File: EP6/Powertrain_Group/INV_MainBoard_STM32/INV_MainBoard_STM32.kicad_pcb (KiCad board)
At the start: 4 copper layers, 100 x 88 mm, 290 parts, among them J1 FX26-30P-1SV, J10 current_DC, J11 current_U, J12 current_V, J13 current_W, J2 motorSense, J3 LVBattery, J4 STDC14, J5 current_DC, J6 current_U, J7 current_V, J8 current_V, J9 CAN, SW1 TS-1187A-B-A-B, U1 OPA340NA, U10 OPA340NA, U11 OPA340NA, U12 OPA340NA, U13 LMV7219M5, U14 LMV7219M5, U15 LMV7219M5, U16 LMV7219M5, U17 LMV7219M5, U18 LMV7219M5, U19 LMV7219M5, U2 TPS5430DDAR, U20 LMV7219M5, U21 OPA340NA, U22 TCAN1042VDRQ1, U3 AMS1117-3.3, U4 STM32G474RETx, U5 CAT24C256, U6 TCAN1042VDRQ1, U7 OPA340NA, U8 OPA340NA, U9 OPA340NA, Y1 X322525MOB4SI 25Mhz, Y2 X322516MLB4SI 16MHz

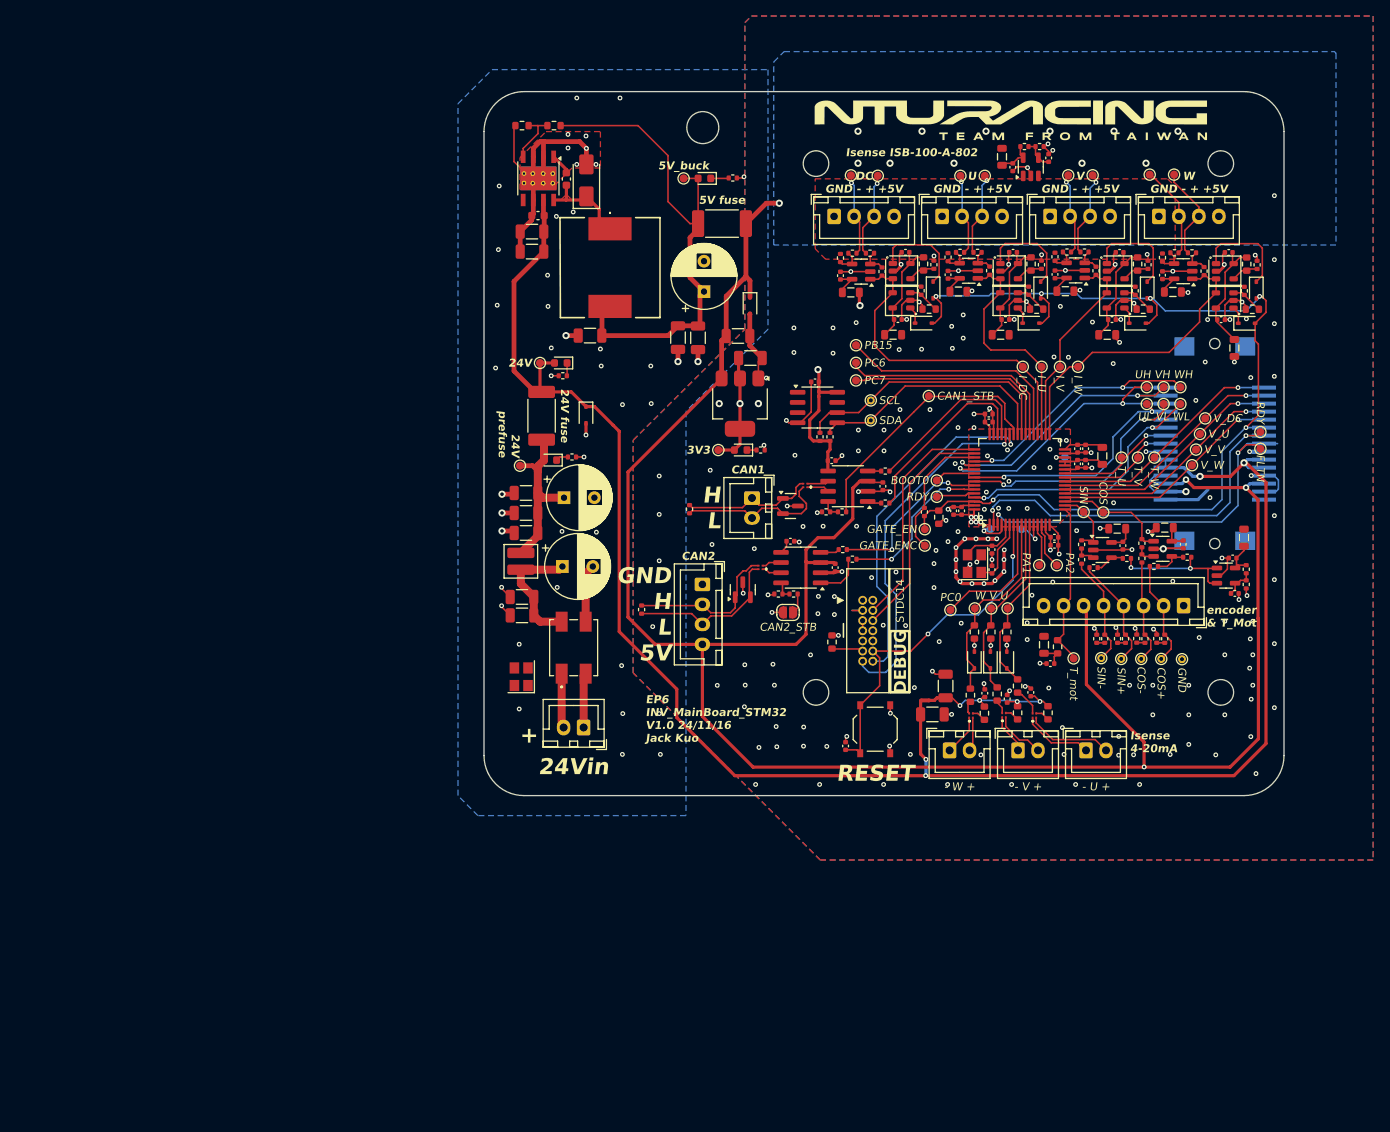
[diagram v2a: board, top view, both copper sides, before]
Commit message: update INV_MainBoard_STM32 to V2.0
big update to match new INV_GateDriver
and use H743ZI as MCU
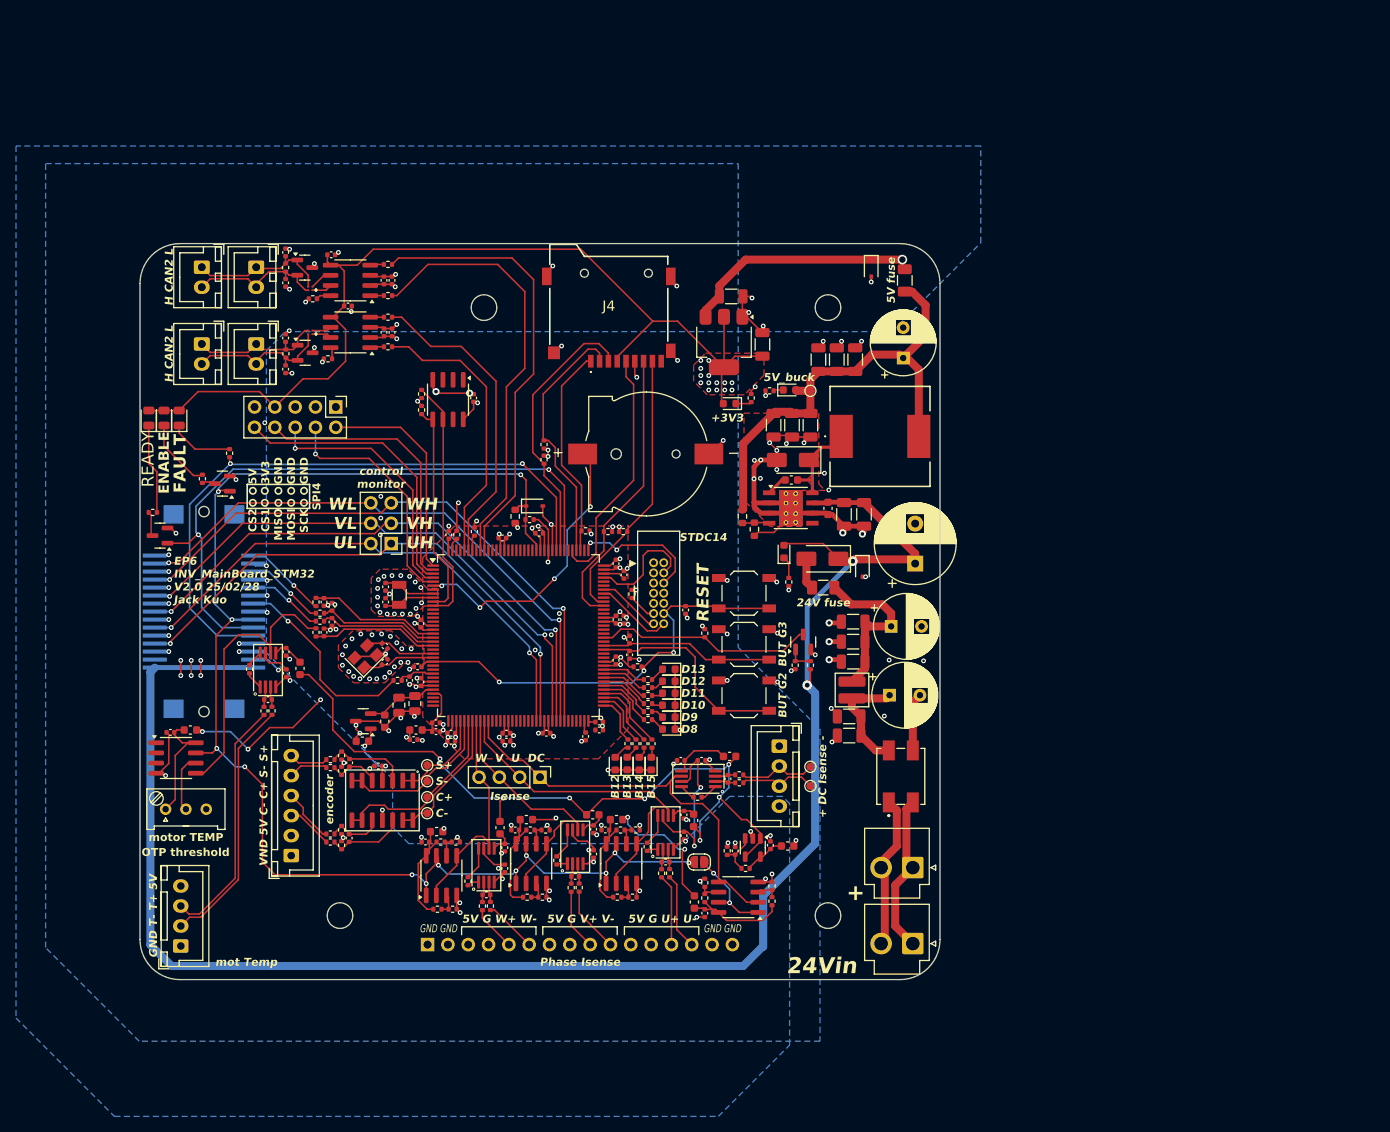
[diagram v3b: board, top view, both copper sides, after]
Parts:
- removed FB17: GZ1608D601TF, Inductor_SMD:L_0805_2012Metric
- removed FB3: GZ2012D601TF, Inductor_SMD:L_0805_2012Metric
- removed FL4, FL5, FL6: EXC-X4CE900U, SamacSys_Parts_EP6:EXCX4CE900U
- removed H5: M4, MountingHole:MountingHole_4mm
- removed TIE1, TIE2: NetTie, NetTie:NetTie-2_SMD_Pad0.5mm
- removed TP1: 24V_prefuse, TestPoint:TestPoint_Pad_D1.0mm
- removed TP10: A1, TestPoint:TestPoint_Pad_D1.0mm
- removed TP11: A2, TestPoint:TestPoint_Pad_D1.0mm
- removed TP12: eCOS, TestPoint:TestPoint_Pad_D1.0mm
- removed TP13: B7, TestPoint:TestPoint_Pad_D1.0mm
- removed TP14: B10, TestPoint:TestPoint_Pad_D1.0mm
- removed TP15: B15, TestPoint:TestPoint_Pad_D1.0mm
- removed TP16: D2, TestPoint:TestPoint_Pad_D1.0mm
- removed TP17: C6, TestPoint:TestPoint_Pad_D1.0mm
- removed TP18: C7, TestPoint:TestPoint_Pad_D1.0mm
- removed TP19: C15, TestPoint:TestPoint_Pad_D1.0mm
- removed TP2: 24V, TestPoint:TestPoint_Pad_D1.0mm
- removed TP20: C0, TestPoint:TestPoint_Pad_D1.0mm
- removed TP21: eSIN, TestPoint:TestPoint_Pad_D1.0mm
- removed TP22: WH, TestPoint:TestPoint_Pad_D1.0mm
- removed TP23: VH, TestPoint:TestPoint_Pad_D1.0mm
- removed TP24: UH, TestPoint:TestPoint_Pad_D1.0mm
- removed TP25: Ready, TestPoint:TestPoint_Pad_D1.0mm
- removed TP26: NFLT, TestPoint:TestPoint_Pad_D1.0mm
- removed TP27: GEnC, TestPoint:TestPoint_Pad_D1.0mm
- removed TP28: CAN1_STB, TestPoint:TestPoint_Pad_D1.0mm
- removed TP29: TW, TestPoint:TestPoint_Pad_D1.0mm
- removed TP30: TV, TestPoint:TestPoint_Pad_D1.0mm
- removed TP31: TU, TestPoint:TestPoint_Pad_D1.0mm
- removed TP32: UL, TestPoint:TestPoint_Pad_D1.0mm
- removed TP33: VL, TestPoint:TestPoint_Pad_D1.0mm
- removed TP34: WL, TestPoint:TestPoint_Pad_D1.0mm
- removed TP35: GEnFb, TestPoint:TestPoint_Pad_D1.0mm
- removed TP36: IW, TestPoint:TestPoint_Pad_D1.0mm
- removed TP37: IV, TestPoint:TestPoint_Pad_D1.0mm
- removed TP38: IU, TestPoint:TestPoint_Pad_D1.0mm
- removed TP39: IDC, TestPoint:TestPoint_Pad_D1.0mm
- removed TP4: 3V3, TestPoint:TestPoint_Pad_D1.0mm
- removed TP40: IcW, TestPoint:TestPoint_Pad_D1.0mm
- removed TP41: IcV, TestPoint:TestPoint_Pad_D1.0mm
- removed TP42: IcU, TestPoint:TestPoint_Pad_D1.0mm
- removed TP43: VU, TestPoint:TestPoint_Pad_D1.0mm
- removed TP44: VDC, TestPoint:TestPoint_Pad_D1.0mm
- removed TP45: VV, TestPoint:TestPoint_Pad_D1.0mm
- removed TP46: VW, TestPoint:TestPoint_Pad_D1.0mm
- removed TP47: TM, TestPoint:TestPoint_Pad_D1.0mm
- removed TP48: GND, TestPoint:TestPoint_THTPad_D1.0mm_Drill0.5mm
- removed TP49: SCL, TestPoint:TestPoint_THTPad_D1.0mm_Drill0.5mm
- removed TP50: SDA, TestPoint:TestPoint_THTPad_D1.0mm_Drill0.5mm
- removed TP53: I_U+, TestPoint:TestPoint_Pad_D1.0mm
- removed TP54: I_U-, TestPoint:TestPoint_Pad_D1.0mm
- removed TP55: I_V+, TestPoint:TestPoint_Pad_D1.0mm
- removed TP56: I_V-, TestPoint:TestPoint_Pad_D1.0mm
- removed TP57: I_W+, TestPoint:TestPoint_Pad_D1.0mm
- removed TP58: I_W-, TestPoint:TestPoint_Pad_D1.0mm
- removed TP9: A0, TestPoint:TestPoint_Pad_D1.0mm
- removed U19, U20: LMV7219M5, PCM_Package_TO_SOT_SMD_AKL:SOT-23-5
- removed U21: OPA340NA, Package_TO_SOT_SMD:SOT-23-5
- removed U22: TCAN1042VDRQ1, Package_SO:SOIC-8_3.9x4.9mm_P1.27mm
- added BT1: 1056, nturt_kicad_lib_EP6:BAT_1056, F.Cu at (172.0, 83.3)
- added C100: 680p, Capacitor_SMD:C_0402_1005Metric, F.Cu at (174.2, 134.3)
- added C101: 680p, Capacitor_SMD:C_0402_1005Metric, F.Cu at (162.9, 136.1)
- added C102: 680p, Capacitor_SMD:C_0402_1005Metric, F.Cu at (151.8, 138.4)
- added C103: 100n, Capacitor_SMD:C_0402_1005Metric, F.Cu at (187.3, 132.2)
- added C104: 100n, Capacitor_SMD:C_0402_1005Metric, F.Cu at (182.9, 132.9)
- added C105: 100n, Capacitor_SMD:C_0402_1005Metric, F.Cu at (126.8, 108.0)
- added C106: 100n, Capacitor_SMD:C_0402_1005Metric, F.Cu at (176.1, 121.6)
- added C107: 100n, Capacitor_SMD:C_0402_1005Metric, F.Cu at (176.5, 128.4)
- added C108: 100n, Capacitor_SMD:C_0402_1005Metric, F.Cu at (165.2, 130.2)
- added C109: 100n, Capacitor_SMD:C_0402_1005Metric, F.Cu at (154.1, 132.5)
- added C112: 22p, Capacitor_SMD:C_0402_1005Metric, F.Cu at (126.7, 58.1)
- added C113: 22p, Capacitor_SMD:C_0402_1005Metric, F.Cu at (126.7, 61.9)
- added C114: 22p, Capacitor_SMD:C_0402_1005Metric, F.Cu at (126.7, 68.8)
- added C115: 22p, Capacitor_SMD:C_0402_1005Metric, F.Cu at (126.7, 72.7)
- added C116: 4u7 10v, Capacitor_SMD:C_0402_1005Metric, F.Cu at (140.0, 61.6)
- added C117: 4u7 10v, Capacitor_SMD:C_0402_1005Metric, F.Cu at (140.0, 68.1)
- added C118: 22u 25V, Capacitor_SMD:C_1206_3216Metric, F.Cu at (193.3, 71.5)
- added C119: 22u 25V, Capacitor_SMD:C_1206_3216Metric, F.Cu at (195.6, 71.5)
- added C120: 22u 25V, Capacitor_SMD:C_1206_3216Metric, F.Cu at (197.9, 71.5)
- added C60: 100n, Capacitor_SMD:C_0402_1005Metric, F.Cu at (168.0, 97.0)
- added C61: 100n, Capacitor_SMD:C_0402_1005Metric, F.Cu at (168.0, 104.0)
- added C62: 100n, Capacitor_SMD:C_0402_1005Metric, F.Cu at (147.1, 93.4)
- added C63: 100n, Capacitor_SMD:C_0402_1005Metric, F.Cu at (165.9, 116.8)
- added C64: 0u1, Capacitor_SMD:C_0402_1005Metric, F.Cu at (145.5, 116.9)
- added C65: 10u 6V, Capacitor_SMD:C_0402_1005Metric, F.Cu at (145.5, 118.0)
- added C66: 10u 6V, Capacitor_SMD:C_0402_1005Metric, F.Cu at (142.7, 119.0)
- added C67: 4u7, Capacitor_SMD:C_0402_1005Metric, F.Cu at (154.3, 119.2)
- added C85: 43p, Capacitor_SMD:C_0402_1005Metric, F.Cu at (134.6, 131.3)
- added C86: 100n, Capacitor_SMD:C_0402_1005Metric, F.Cu at (138.3, 122.3)
- added C87: 22u, Capacitor_SMD:C_0805_2012Metric, F.Cu at (140.9, 114.7)
- added C88: 22u, Capacitor_SMD:C_0805_2012Metric, F.Cu at (142.9, 114.5)
- added C91: 470n, Capacitor_SMD:C_0603_1608Metric, F.Cu at (139.1, 116.7)
- added C92: 470n, Capacitor_SMD:C_0603_1608Metric, F.Cu at (136.3, 119.2)
- added C96: 1u, Capacitor_SMD:C_0402_1005Metric, F.Cu at (124.5, 114.0)
- added C97: 3n3, Capacitor_SMD:C_0402_1005Metric, F.Cu at (142.2, 111.6)
- added C99: 680p, Capacitor_SMD:C_0402_1005Metric, F.Cu at (182.0, 123.9)
- added D21: Y LED, LED_SMD:LED_0603_1608Metric, F.Cu at (169.4, 122.0)
- added D22: G LED, LED_SMD:LED_0603_1608Metric, F.Cu at (170.9, 122.0)
- added D23: B LED, LED_SMD:LED_0603_1608Metric, F.Cu at (172.4, 122.0)
- added J14: LVBattery, Connector_JST:JST_VH_B2P-VH_1x02_P3.96mm_Vertical, F.Cu at (205.1, 144.5)
- added J15: STDC14, nturt_kicad_lib_EP6:box_header_14P_pitch127, F.Cu at (172.7, 96.9)
- added J16: SPI, Connector_PinHeader_2.54mm:PinHeader_2x05_P2.54mm_Vertical, F.Cu at (133.0, 77.4)
- added Q1: 2N7002, Package_TO_SOT_SMD:SOT-23, F.Cu at (118.8, 87.0)
- added Q2: 2N7002, Package_TO_SOT_SMD:SOT-23, F.Cu at (111.0, 93.5)
- added Q3: AO3400A, Package_TO_SOT_SMD:SOT-23, F.Cu at (191.4, 106.8)
- added R84: 15k, Resistor_SMD:R_0402_1005Metric, F.Cu at (192.3, 109.7)
- added R85: 1k, Resistor_SMD:R_0402_1005Metric, F.Cu at (190.4, 109.7)
- added R86: 2k2, Resistor_SMD:R_0402_1005Metric, F.Cu at (170.5, 119.5)
- added R87: 2k2, Resistor_SMD:R_0402_1005Metric, F.Cu at (171.5, 119.5)
- added R88: 2k2, Resistor_SMD:R_0402_1005Metric, F.Cu at (172.5, 119.5)
- added RV1: 10K, nturt_kicad_lib_EP6:Throughhole Potentiometer 3296W, F.Cu at (111.7, 127.7)
- added SW2: TS-1187A-B-A-B, Button_Switch_SMD:SW_SPST_TL3342, F.Cu at (184.0, 107.1)
- added SW3: TS-1187A-B-A-B, Button_Switch_SMD:SW_SPST_TL3342, F.Cu at (184.0, 113.5)
- added U23: REF3133AQDBZRQ1, Package_TO_SOT_SMD:SOT-23, F.Cu at (136.4, 116.7)
- C1, C2: value 0u1 -> 47u 10V; footprint Capacitor_SMD:C_0402_1005Metric -> Capacitor_SMD:C_1206_3216Metric
- C20, C21: value 47u 10V -> 100n; footprint Capacitor_SMD:C_1206_3216Metric -> Capacitor_SMD:C_0402_1005Metric
- C22, C23, C24, C25: value 10u 6V -> 100n
- C26, C27, C29, C38, C40, C41, C42, C43, C46, C47, C48, C49, C51, C52, C57, C58: value 0u1 -> 100n
- C28: value 0u1 -> 4u7
- C30: value 0u1 -> 15p
- C31: value 10u 6V -> 15p
- C33, C34: value 15p -> 27p
- C44, C45: value 0u1 -> 2u2
- C54: value 0u1 -> 100uF 27V; footprint Capacitor_SMD:C_0402_1005Metric -> Capacitor_THT:CP_Radial_D10.0mm_P5.00mm
- C55, C56: value 10u 35V -> 4u7; footprint Capacitor_SMD:C_1206_3216Metric -> Capacitor_SMD:C_0402_1005Metric
- C59: value 0u1 -> 43p
- D1: value RED 24VpreFuse -> GREEN LED; footprint LED_SMD:LED_0603_1608Metric -> LED_SMD:LED_0805_2012Metric
- D10: value 1N4148W -> G LED; footprint Diode_SMD:D_SOD-323 -> LED_SMD:LED_0603_1608Metric
- D11: value 1N4148W -> R LED; footprint Diode_SMD:D_SOD-323 -> LED_SMD:LED_0603_1608Metric
- D12: value 1N4148W -> RED 3V3; footprint Diode_SMD:D_SOD-323 -> LED_SMD:LED_0603_1608Metric
- D13: value 1N4148W -> B LED; footprint Diode_SMD:D_SOD-323 -> LED_SMD:LED_0603_1608Metric
- D14: value 1N4148W -> Y LED; footprint Diode_SMD:D_SOD-323 -> LED_SMD:LED_0603_1608Metric
- D15: value 1N4148W -> B5818WS
- D16: value 1N4148W -> W LED; footprint Diode_SMD:D_SOD-323 -> LED_SMD:LED_0603_1608Metric
- D18, D20: value 3.7V BZT52C3V9S -> R LED; footprint Diode_SMD:D_SOD-323 -> LED_SMD:LED_0603_1608Metric
- D19: value 3.7V BZT52C3V9S -> SS54; footprint Diode_SMD:D_SOD-323 -> Diode_SMD:D_SMA
- D7: value RED 3V3 -> WHITE LED; footprint LED_SMD:LED_0603_1608Metric -> LED_SMD:LED_0805_2012Metric
- D9: value 1N4148W -> RED; footprint Diode_SMD:D_SOD-323 -> LED_SMD:LED_0805_2012Metric
- F1: footprint Fuse:Fuse_2512_6332Metric_Pad1.52x3.35mm_HandSolder -> Fuse:Fuse_1206_3216Metric
- F2: value 0.5A -> 1A; footprint Fuse:Fuse_2512_6332Metric_Pad1.52x3.35mm_HandSolder -> Fuse:Fuse_1206_3216Metric
- FB1, FB10, FB11, FB13, FB15, FB2, FB4, FB5, FB6, FB7, FB8, FB9: value GZ2012D601TF -> GZ1608D601TF; footprint Inductor_SMD:L_0805_2012Metric -> Capacitor_SMD:C_0603_1608Metric
- J10: value current_DC -> CAN; footprint Connector_JST:JST_XH_B4B-XH-A_1x04_P2.50mm_Vertical -> Connector_JST:JST_XH_B2B-XH-A_1x02_P2.50mm_Vertical
- J11: value current_U -> CAN
- J12: value current_V -> CAN
- J13: value current_W -> motorTemp; footprint Connector_JST:JST_XH_B2B-XH-A_1x02_P2.50mm_Vertical -> Connector_JST:JST_XH_B4B-XH-A_1x04_P2.50mm_Vertical
- J2: footprint Connector_JST:JST_XH_B8B-XH-A_1x08_P2.50mm_Vertical -> Connector_JST:JST_XH_B6B-XH-A_1x06_P2.50mm_Vertical
- J3: footprint Connector_JST:JST_XH_B2B-XH-A_1x02_P2.50mm_Vertical -> Connector_JST:JST_VH_B2P-VH_1x02_P3.96mm_Vertical
- J4: value STDC14 -> MSD-4-A; footprint nturt_kicad_lib_EP6:box_header_14P_pitch127 -> SamacSys_Parts_EP6:MSD4A
- J6: value current_U -> to PhaseIsense; footprint Connector_JST:JST_XH_B4B-XH-A_1x04_P2.50mm_Vertical -> Connector_PinHeader_2.54mm:PinHeader_1x16_P2.54mm_Horizontal; moved to B.Cu
- J7: value current_V -> phase control monitor; footprint Connector_JST:JST_XH_B4B-XH-A_1x04_P2.50mm_Vertical -> Connector_PinHeader_2.54mm:PinHeader_2x03_P2.54mm_Vertical
- J8: value current_V -> current; footprint Connector_JST:JST_XH_B4B-XH-A_1x04_P2.50mm_Vertical -> Connector_PinHeader_2.54mm:PinHeader_1x04_P2.54mm_Vertical
- JP1: value CAN2STB -> DC OCP
- L3: footprint SamacSys_Parts:SRR1260A220M -> SamacSys_Parts_EP6:SRR1260A220M
- R1: value 10k -> 510R
- R11: value 1k -> 10k
- R12: value 100R -> 4k7; footprint Resistor_SMD:R_0603_1608Metric -> Resistor_SMD:R_0402_1005Metric
- R13, R14, R18, R28, R6, R68: value 10k -> 2k2
- R15, R16, R70, R71: value 100R -> 20R
- R17: value 100R -> 90R
- R19, R20, R21, R22: value 10k -> 10k 0.1%
- R2: value 10k -> 100R
- R23: value 20k -> 20k 0.1%
- R24: value 20k -> 4k7
- R25, R26: value 20k -> 10k 0.1%
- R27: value 15k -> 2k2
- R29, R55: value 10k -> 2k4
- R3: value 20k -> 1k
- R30, R31, R50: value 15k -> 10k
- R33, R51, R58: value 10k -> 28k
- R34, R38: value 15k -> 20k 0.1%
- R35, R39, R43, R47: value 15k -> 100R
- R36, R40, R44, R48: value 20k -> 100R
- R37: value 20k -> 10M
- R41, R45, R49: value 20k -> 100k
- R42, R46: value 15k -> 4k7
- R5: value 1k -> 10k; footprint Resistor_SMD:R_0603_1608Metric -> Resistor_SMD:R_0402_1005Metric
- R52, R57, R61, R64: value 45k3 -> 10k; footprint Resistor_SMD:R_0603_1608Metric -> Resistor_SMD:R_0402_1005Metric
- R53, R56, R60: value 45k3 -> 28k; footprint Resistor_SMD:R_0603_1608Metric -> Resistor_SMD:R_0402_1005Metric
- R62: value 10k -> 4k7
- R65: value 45k3 -> 10M; footprint Resistor_SMD:R_0603_1608Metric -> Resistor_SMD:R_0402_1005Metric
- R67: value 120R -> 10k
- R72: value 120R -> 90R
- R73: value 100R -> 10k
- R75: value 150R -> 100R; footprint Resistor_SMD:R_0603_1608Metric -> Resistor_SMD:R_0402_1005Metric
- R76: value 150R -> 1k; footprint Resistor_SMD:R_0603_1608Metric -> Resistor_SMD:R_0402_1005Metric
- R77: value 150R -> 2k2; footprint Resistor_SMD:R_0603_1608Metric -> Resistor_SMD:R_0402_1005Metric
- R78, R80: value 100R -> 2k2; footprint Resistor_SMD:R_0603_1608Metric -> Resistor_SMD:R_0402_1005Metric
- R79: value 100R -> 10k; footprint Resistor_SMD:R_0603_1608Metric -> Resistor_SMD:R_0402_1005Metric
- R81, R82: value 100R -> 1k; footprint Resistor_SMD:R_0603_1608Metric -> Resistor_SMD:R_0402_1005Metric
- R83: value 100R -> 20k 0.1%; footprint Resistor_SMD:R_0603_1608Metric -> Resistor_SMD:R_0402_1005Metric
- SW1: footprint Button_Switch_SMD:SW_Push_1P1T_XKB_TS-1187A -> Button_Switch_SMD:SW_SPST_TL3342
- TP5, TP6, TP7, TP8: footprint TestPoint:TestPoint_THTPad_D1.0mm_Drill0.5mm -> TestPoint:TestPoint_Pad_D1.0mm
- TP51: value I_DC+ -> I_W+
- TP52: value I_DC- -> I_W-
- U1: value OPA340NA -> STM32H743ZITx; footprint Package_TO_SOT_SMD:SOT-23-5 -> Package_QFP:LQFP-144_20x20mm_P0.5mm
- U10, U11, U12: value OPA340NA -> LM2903; footprint Package_TO_SOT_SMD:SOT-23-5 -> Package_SO:SOIC-8_3.9x4.9mm_P1.27mm
- U13, U15: value LMV7219M5 -> LM2903; footprint PCM_Package_TO_SOT_SMD_AKL:SOT-23-5 -> Package_SO:SOIC-8_3.9x4.9mm_P1.27mm
- U14: value LMV7219M5 -> INA333AIDGK; footprint PCM_Package_TO_SOT_SMD_AKL:SOT-23-5 -> PCM_Package_SO_AKL:MSOP-8_3x3mm_P0.65mm
- U16: value LMV7219M5 -> LM324D; footprint PCM_Package_TO_SOT_SMD_AKL:SOT-23-5 -> PCM_Package_SO_AKL:SOIC-14_3.9x8.7mm_P1.27mm
- U17: value LMV7219M5 -> AMS1117-3.3; footprint PCM_Package_TO_SOT_SMD_AKL:SOT-23-5 -> Package_TO_SOT_SMD:SOT-223-3_TabPin2
- U18: value LMV7219M5 -> OPA340NA; footprint PCM_Package_TO_SOT_SMD_AKL:SOT-23-5 -> Package_TO_SOT_SMD:SOT-23-5
- U3: value AMS1117-3.3 -> INA333AIDGK; footprint Package_TO_SOT_SMD:SOT-223-3_TabPin2 -> PCM_Package_SO_AKL:MSOP-8_3x3mm_P0.65mm
- U4: value STM32G474RETx -> TCAN1042VDRQ1; footprint Package_QFP:LQFP-64_10x10mm_P0.5mm -> Package_SO:SOIC-8_3.9x4.9mm_P1.27mm
- U7, U8, U9: value OPA340NA -> INA333AIDGK; footprint Package_TO_SOT_SMD:SOT-23-5 -> PCM_Package_SO_AKL:MSOP-8_3x3mm_P0.65mm
- Y1: value X322525MOB4SI 25Mhz -> 48MHz YF4048M00033T8188103
- Y2: value X322516MLB4SI 16MHz -> 32.768kHz Q13FC13500004; footprint Crystal:Crystal_SMD_3225-4Pin_3.2x2.5mm -> Crystal:Crystal_SMD_3215-2Pin_3.2x1.5mm
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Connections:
- C1 pad 1: Net-(U1-V+) -> +5V
- C2 pad 1: Net-(U1--) -> +3V3
- C20 pad 1: +5V -> /Isense&motT_OCP&OTP/filt3V3
- C21 pad 1: +3V3 -> +5V
- C30 pad 1: /MCU/3V3_REF -> /MCU/OSC32_OUT
- C31 pad 1: /MCU/3V3_REF -> /MCU/OSC32_IN
- C32 pad 1: /MCU/SWD_NRST -> /MCU/NRST
- C33 pad 1: /MCU/OSC_IN -> /MCU/OSC_OUT
- C33 pad 2: /MCU/CrystalGND -> GND
- C34 pad 1: /MCU/OSC_OUT -> /MCU/OSC_IN
- C34 pad 2: /MCU/CrystalGND -> GND
- C38 pad 1: Net-(U7-V+) -> /T_filt_mot
- C39 pad 1: Net-(U8-V+) -> /MCU/BUT_G3
- C40 pad 1: Net-(U9-V+) -> +5V
- C41 pad 1: Net-(U10-V+) -> +5V
- C42 pad 1: Net-(U11-V+) -> +5V
- C43 pad 1: Net-(U12-V+) -> +5V
- C44 pad 1: Net-(U13-V+) -> /MCU/VCAP1
- C45 pad 1: Net-(U13-V+) -> /MCU/VCAP2
- C46 pad 1: Net-(U15-V+) -> /Isense&motT_OCP&OTP/OCPnode/filt3V3
- C47 pad 1: Net-(U15-V+) -> /Isense&motT_OCP&OTP/OCPnode1/filt3V3
- C48 pad 1: Net-(U17-V+) -> /Isense&motT_OCP&OTP/OCPnode2/filt3V3
- C49 pad 1: Net-(U17-V+) -> /Isense&motT_OCP&OTP/OCPnode3/filt3V3
- C50 pad 1: Net-(U19-V+) -> /MCU/NRST
- C51 pad 1: Net-(U19-V+) -> +3V3
- C52 pad 1: Net-(C52-Pad1) -> /T_filt_W
- C53 pad 1: Net-(U21-V+) -> /MCU/BUT_G2
- C54 pad 1: Net-(U21--) -> +24V
- C55 pad 1: +24V -> +3V3
- C56 pad 1: /Isense_OCP/+24V_4-20mA -> +3V3
- C57 pad 1: /Isense_OCP/+24V_4-20mA -> /T_filt_V
- C58 pad 1: /Isense_OCP/+24V_4-20mA -> /T_filt_U
- C59 pad 1: /Isense_OCP/+24V_4-20mA -> Net-(U16A-+)
- C59 pad 2: GND -> Net-(U16B-+)
- D1 pad 2: /Power/+24V_prefuse -> +3V3
- D10 pad 1: Net-(D10-K) -> GND
- D10 pad 2: /GATE_EN -> Net-(D10-A)
- D11 pad 1: Net-(D11-K) -> GND
- D11 pad 2: /GATE_EN -> Net-(D11-A)
- D12 pad 2: /GATE_EN -> +3V3
- D13 pad 1: Net-(D13-K) -> GND
- D13 pad 2: /GATE_EN -> Net-(D13-A)
- D14 pad 1: Net-(D14-K) -> GND
- D14 pad 2: /GATE_EN -> Net-(D14-A)
- D15 pad 1: Net-(D15-K) -> /GATE_EN
- D15 pad 2: /GATE_EN -> /OCPFLTN
- D16 pad 1: Net-(D16-K) -> GND
- D16 pad 2: /GATE_EN -> Net-(D16-A)
- D17 pad 1: /MCU/CAN2L -> /Peripherals/CAN1L
- D17 pad 2: /MCU/CAN2H -> /Peripherals/CAN1H
- D18 pad 1: /Isense_OCP/Isense_current_U -> GND
- D18 pad 2: GND -> Net-(D18-A)
- D19 pad 1: /Isense_OCP/Isense_current_V -> +24V
- D19 pad 2: GND -> Net-(D19-A)
- D20 pad 1: /Isense_OCP/Isense_current_W -> GND
- D20 pad 2: GND -> Net-(D20-A)
- D8 pad 1: /MCU/CAN1L -> /Peripherals/CAN2L
- D8 pad 2: /MCU/CAN1H -> /Peripherals/CAN2H
- D9 pad 2: /GATE_EN -> +3V3
- F1 pad 2: +24V -> Net-(D19-A)
- FB1 pad 2: Net-(U1-V+) -> /Isense&motT_OCP&OTP/OCPnode/filt3V3
- FB10 pad 1: +3V3 -> Net-(U8-REF)
- FB10 pad 2: Net-(U21-V+) -> /Isense&motT_OCP&OTP/Vref_1.65V
- FB11 pad 2: Net-(U15-V+) -> /Isense&motT_OCP&OTP/filt3V3
- FB13 pad 1: +3V3 -> Net-(U9-REF)
- FB13 pad 2: Net-(U17-V+) -> /Isense&motT_OCP&OTP/Vref_1.65V
- FB15 pad 1: +3V3 -> Net-(U14-REF)
- FB15 pad 2: Net-(U19-V+) -> /Isense&motT_OCP&OTP/Vref_1.65V
- FB2 pad 1: +3V3 -> /MCU/VDDA_MCU
- FB2 pad 2: /MCU/3V3_REF -> +3V3
- FB4 pad 2: Net-(U8-V+) -> Net-(U18-V+)
- FB5 pad 1: +3V3 -> Net-(U3-REF)
- FB5 pad 2: Net-(U9-V+) -> /Isense&motT_OCP&OTP/Vref_1.65V
- FB6 pad 1: +3V3 -> Net-(U7-REF)
- FB6 pad 2: Net-(U10-V+) -> /Isense&motT_OCP&OTP/Vref_1.65V
- FB7 pad 2: Net-(U11-V+) -> /Isense&motT_OCP&OTP/OCPnode1/filt3V3
- FB8 pad 2: Net-(U12-V+) -> /Isense&motT_OCP&OTP/OCPnode2/filt3V3
- FB9 pad 2: Net-(U13-V+) -> /Isense&motT_OCP&OTP/OCPnode3/filt3V3
- FL2 pad 1: Net-(U6-CANH) -> Net-(U4-CANH)
- FL2 pad 2: Net-(U6-CANL) -> Net-(U4-CANL)
- FL2 pad 3: /MCU/CAN1L -> /Peripherals/CAN2L
- FL2 pad 4: /MCU/CAN1H -> /Peripherals/CAN2H
- FL3 pad 1: Net-(U22-CANH) -> Net-(U6-CANH)
- FL3 pad 2: Net-(U22-CANL) -> Net-(U6-CANL)
- FL3 pad 3: /MCU/CAN2L -> /Peripherals/CAN1L
- FL3 pad 4: /MCU/CAN2H -> /Peripherals/CAN1H
- J1 pad 1: +3V3 -> +24V
- J1 pad 10: +24V -> /FLTN
- J1 pad 11: +24V -> /UL
- J1 pad 12: +24V -> /RDY
- J1 pad 14: GND -> /GATE_EN
- J1 pad 15: /T_V -> /VH
- J1 pad 16: /FLTN -> GND
- J1 pad 17: /T_U -> GND
- J1 pad 18: /RDY -> /Vsense_DC
- J1 pad 19: /WL -> /VL
- J1 pad 2: +3V3 -> +24V
- J1 pad 20: /GATE_EN -> GND
- J1 pad 21: /VL -> GND
- J1 pad 22: /Vsense_W -> /T_W
- J1 pad 23: /UL -> /WH
- J1 pad 24: /Vsense_V -> GND
- J1 pad 25: /UH -> GND
- J1 pad 26: /Vsense_U -> /T_V
- J1 pad 27: /VH -> /WL
- J1 pad 28: /Vsense_DC -> GND
- J1 pad 29: /WH -> GND
- J1 pad 3: GND -> +5V
- J1 pad 30: /T_W -> /T_U
- J1 pad 4: GND -> +5V
- J1 pad 5: +5V -> GND
- J1 pad 6: +5V -> GND
- J1 pad 7: GND -> /UH
- J1 pad 9: +24V -> GND
- J10 pad 1: GND -> /Peripherals/CAN2L
- J10 pad 2: /MCU/CAN2L -> /Peripherals/CAN2H
- J11 pad 1: Net-(J11-Pin_1) -> /Peripherals/CAN1L
- J11 pad 2: Net-(J11-Pin_2) -> /Peripherals/CAN1H
- J12 pad 1: Net-(J12-Pin_1) -> /Peripherals/CAN1L
- J12 pad 2: Net-(J12-Pin_2) -> /Peripherals/CAN1H
- J13 pad 1: Net-(J13-Pin_1) -> GND
- J13 pad 2: Net-(J13-Pin_2) -> /Isense&motT_OCP&OTP/MotTempNode/IN-
- J2 pad 2: /COS- -> +5V
- J2 pad 3: /COS+ -> /COS-
- J2 pad 4: /SIN- -> /COS+
- J2 pad 5: /SIN+ -> /SIN-
- J2 pad 6: +5V -> /SIN+
- J4 pad 1: unconnected-(J4-Pin_1-Pad1) -> /MCU/SDMMC1_D2
- J4 pad 2: unconnected-(J4-Pin_2-Pad2) -> /MCU/SDMMC1_D3
- J4 pad 3: +3V3 -> /MCU/SDMMC1_CMD
- J4 pad 4: /MCU/SWD_SWDIO -> +3V3
- J4 pad 5: GND -> /MCU/SDMMC1_CK
- J4 pad 6: /MCU/SWD_SWCLK -> GND
- J4 pad 7: GND -> /MCU/SDMMC1_D0
- J4 pad 8: unconnected-(J4-Pin_8-Pad8) -> /MCU/SDMMC1_D1
- J5 pad 2: /Isense_OCP/IsenseNode/IN- -> /Isense&motT_OCP&OTP/IsenseNode/IN-
- J5 pad 3: /Isense_OCP/IsenseNode/IN+ -> /Isense&motT_OCP&OTP/IsenseNode/IN+
- J6 pad 2: /Isense_OCP/IsenseNode1/IN- -> GND
- J6 pad 3: /Isense_OCP/IsenseNode1/IN+ -> +5V
- J6 pad 4: +5V -> GND
- J7 pad 1: GND -> /UH
- J7 pad 2: /Isense_OCP/IsenseNode2/IN- -> /UL
- J7 pad 3: /Isense_OCP/IsenseNode2/IN+ -> /VH
- J7 pad 4: +5V -> /VL
- J8 pad 1: GND -> /Isense&motT_OCP&OTP/Isense_DC
- J8 pad 2: /Isense_OCP/IsenseNode3/IN- -> /Isense&motT_OCP&OTP/Isense_U
- J8 pad 3: /Isense_OCP/IsenseNode3/IN+ -> /Isense&motT_OCP&OTP/Isense_V
- J8 pad 4: +5V -> /Isense&motT_OCP&OTP/Isense_W
- J9 pad 1: /MCU/CAN1L -> /Peripherals/CAN2L
- J9 pad 2: /MCU/CAN1H -> /Peripherals/CAN2H
- JP1 pad 1: /MCU/CAN2_STB -> /Isense&motT_OCP&OTP/OCPnode/GateEnable
- JP1 pad 2: +3V3 -> /GATE_EN
- R1 pad 1: Net-(U1-V+) -> Net-(D12-K)
- R1 pad 2: Net-(U1--) -> GND
- R11 pad 1: Net-(D7-K) -> /T_V
- R11 pad 2: GND -> /T_filt_V
- R12 pad 1: GND -> /MCU/SDMMC1_D0
- R12 pad 2: /MCU/GNDDetect -> +3V3
- R13 pad 1: +3V3 -> /MCU/LED_D11
- R13 pad 2: /MCU/I2C_SDA -> Net-(D13-A)
- R14 pad 1: +3V3 -> /MCU/LED_D12
- R14 pad 2: /MCU/I2C_SCL -> Net-(D16-A)
- R15 pad 1: /MCU/CAN1_TX -> /MCU/CAN2_TX
- R15 pad 2: Net-(U6-TXD) -> Net-(U4-TXD)
- R16 pad 1: /MCU/CAN1_RX -> /MCU/CAN2_RX
- R16 pad 2: Net-(U6-RXD) -> Net-(U4-RXD)
- R17 pad 1: /MCU/CAN1_STB -> /Peripherals/CAN2H
- R17 pad 2: Net-(U6-STB) -> /Peripherals/CAN2L
- R18 pad 1: Net-(U6-STB) -> /MCU/LED_D13
- R18 pad 2: GND -> Net-(D18-A)
- R19 pad 1: /SIN- -> /SIN+
- R19 pad 2: /EncoderDifVconverter/sin+3V3_out -> Net-(U16A-+)
- R2 pad 1: Net-(U1--) -> /T_mot
- R2 pad 2: GND -> /T_filt_mot
- R20 pad 1: /SIN+ -> /SIN-
- R20 pad 2: /EncoderDifVconverter/sin-3V3_out -> Net-(U16B-+)
- R21 pad 2: /EncoderDifVconverter/cos+3V3_out -> Net-(U16C-+)
- R22 pad 2: /EncoderDifVconverter/cos-3V3_out -> Net-(U16D-+)
- R23 pad 1: /EncoderDifVconverter/sin+3V3_out -> Net-(U16D-+)
- R24 pad 1: /EncoderDifVconverter/sin-3V3_out -> /MCU/SDMMC1_D1
- R24 pad 2: GND -> +3V3
- R25 pad 1: /EncoderDifVconverter/cos+3V3_out -> Net-(U18-V+)
- R25 pad 2: GND -> Net-(U18-+)
- R26 pad 1: /EncoderDifVconverter/cos-3V3_out -> Net-(U18-+)
- R27 pad 1: Net-(U7-+) -> Net-(D7-K)
- R27 pad 2: /EncoderDifVconverter/sin_out -> Net-(Q2-D)
- R28 pad 1: /SIN+ -> Net-(D9-K)
- R28 pad 2: Net-(U7-+) -> /FLTN
- R29 pad 1: /SIN- -> /Isense&motT_OCP&OTP/OCPnode/filt3V3
- R29 pad 2: Net-(U7--) -> Net-(U10A-+)
- R30 pad 1: Net-(U7--) -> Net-(U10A-+)
- R30 pad 2: /EncoderDifVconverter/Vref_1.65V -> GND
- R31 pad 1: Net-(U8-+) -> /Isense&motT_OCP&OTP/OCPnode1/filt3V3
- R31 pad 2: /EncoderDifVconverter/cos_out -> Net-(U11A-+)
- R32 pad 1: /COS+ -> /T_U
- R32 pad 2: Net-(U8-+) -> /T_filt_U
- R33 pad 1: /COS- -> Net-(U11A-+)
- R33 pad 2: Net-(U8--) -> GND
- R34 pad 1: Net-(U8--) -> GND
- R34 pad 2: /EncoderDifVconverter/Vref_1.65V -> Net-(U16C-+)
- R35 pad 1: Net-(U9-+) -> /Isense&motT_OCP&OTP/IsenseNode/IN+
- R35 pad 2: /Isense_OCP/Isense_DC -> Net-(U7--)
- R36 pad 1: /Isense_OCP/IsenseNode/IN+ -> /Isense&motT_OCP&OTP/IsenseNode/IN-
- R36 pad 2: Net-(U9-+) -> Net-(U7-+)
- R37 pad 1: /Isense_OCP/IsenseNode/IN- -> Net-(R37-Pad1)
- R37 pad 2: Net-(U9--) -> Net-(R37-Pad2)
- R38 pad 1: Net-(U9--) -> GND
- R38 pad 2: /Isense_OCP/Vref_1.65V -> Net-(U16A-+)
- R39 pad 1: Net-(U10-+) -> /Isense&motT_OCP&OTP/U+
- R39 pad 2: /Isense_OCP/Isense_U -> Net-(U8--)
- R40 pad 1: /Isense_OCP/IsenseNode1/IN+ -> /Isense&motT_OCP&OTP/U-
- R40 pad 2: Net-(U10-+) -> Net-(U8-+)
- R41 pad 1: /Isense_OCP/IsenseNode1/IN- -> Net-(R41-Pad1)
- R41 pad 2: Net-(U10--) -> Net-(R41-Pad2)
- R42 pad 1: Net-(U10--) -> /MCU/SDMMC1_D2
- R42 pad 2: /Isense_OCP/Vref_1.65V -> +3V3
- R43 pad 1: Net-(U11-+) -> /Isense&motT_OCP&OTP/V+
- R43 pad 2: /Isense_OCP/Isense_V -> Net-(U9--)
- R44 pad 1: /Isense_OCP/IsenseNode2/IN+ -> /Isense&motT_OCP&OTP/V-
- R44 pad 2: Net-(U11-+) -> Net-(U9-+)
- R45 pad 1: /Isense_OCP/IsenseNode2/IN- -> Net-(R45-Pad1)
- R45 pad 2: Net-(U11--) -> Net-(R45-Pad2)
- R46 pad 1: Net-(U11--) -> /MCU/SDMMC1_D3
- R46 pad 2: /Isense_OCP/Vref_1.65V -> +3V3
- R47 pad 1: Net-(U12-+) -> /Isense&motT_OCP&OTP/W+
- R47 pad 2: /Isense_OCP/Isense_W -> Net-(U14--)
- R48 pad 1: /Isense_OCP/IsenseNode3/IN+ -> /Isense&motT_OCP&OTP/W-
- R48 pad 2: Net-(U12-+) -> Net-(U14-+)
- R49 pad 1: /Isense_OCP/IsenseNode3/IN- -> Net-(R49-Pad1)
- R49 pad 2: Net-(U12--) -> Net-(R49-Pad2)
- R5 pad 1: /T_mot -> /T_W
- R5 pad 2: Net-(C52-Pad1) -> /T_filt_W
- R50 pad 1: Net-(U12--) -> /Isense&motT_OCP&OTP/OCPnode2/filt3V3
- R50 pad 2: /Isense_OCP/Vref_1.65V -> Net-(U12A-+)
- R51 pad 1: Net-(U13-V+) -> Net-(U12A-+)
- R51 pad 2: Net-(U13-+) -> GND
- R52 pad 1: Net-(U13-+) -> /Isense&motT_OCP&OTP/OCPnode3/filt3V3
- R52 pad 2: GND -> Net-(U13A-+)
- R53 pad 1: Net-(U13-V+) -> Net-(U13A-+)
- R53 pad 2: Net-(U14--) -> GND
- R54 pad 1: Net-(U14--) -> /Isense&motT_OCP&OTP/OCPnode/filt3V3
- R54 pad 2: GND -> Net-(U10B--)
- R55 pad 1: Net-(U15-V+) -> Net-(U10B--)
- R55 pad 2: Net-(U15-+) -> GND
- R56 pad 1: Net-(U15-+) -> /Isense&motT_OCP&OTP/OCPnode1/filt3V3
- R56 pad 2: GND -> Net-(U11B--)
- R57 pad 1: Net-(U15-V+) -> Net-(U11B--)
- R57 pad 2: Net-(U16--) -> GND
- R58 pad 1: Net-(U16--) -> /Isense&motT_OCP&OTP/OCPnode2/filt3V3
- R58 pad 2: GND -> Net-(U12B--)
- R59 pad 1: Net-(U17-V+) -> Net-(U12B--)
- R59 pad 2: Net-(U17-+) -> GND
- R6 pad 2: GND -> Net-(Q1-D)
- R60 pad 1: Net-(U17-+) -> /Isense&motT_OCP&OTP/OCPnode3/filt3V3
- R60 pad 2: GND -> Net-(U13B--)
- R61 pad 1: Net-(U17-V+) -> Net-(U13B--)
- R61 pad 2: Net-(U18--) -> GND
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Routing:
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- removed copper zone on F.Cu, net /Isense_OCP/Vref_1.65V
- removed copper zone on In1.Cu, net /MCU/CrystalGND
- removed copper zone on B.Cu, net GND
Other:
- board size 100 x 88 mm -> 100 x 92 mm
- board text added: "+ DC Isense -"
- board text added: "+3V3"
- board text added: "5V 3V3 GND GND GND"
- board text added: "5V G U+ U-"
- board text added: "5V G V+ V-"
- board text added: "5V G W+ W-"
- board text added: "B12"
- board text added: "B13"
- board text added: "B14"
- board text added: "B15"
- board text added: "BUT G2"
- board text added: "BUT G3"
- board text added: "C+"
- board text added: "C-"
- board text added: "CS2 CS1 MISO MOSI SCK"
- board text added: "D10"
- board text added: "D11"
- board text added: "D12"
- board text added: "D13"
- board text added: "D8"
- board text added: "D9"
- board text added: "ENABLE"
- board text added: "EP6 INV_MainBoard_STM32 V2.0 25/02/28 Jack Kuo"
- board text added: "FAULT"
- board text added: "GND GND"
- board text added: "GND T- T+ 5V"
- board text added: "H CAN2 L"
- board text added: "Isense"
- board text added: "OTP threshold"
- board text added: "Phase Isense"
- board text added: "READY"
- board text added: "S+"
- board text added: "S-"
- board text added: "SPI4"
- board text added: "VND 5V C- C+ S- S+"
- board text added: "W V U DC"
- board text added: "WH VH UH"
- board text added: "WL VL UL"
- board text added: "control monitor"
- board text added: "encoder"
- board text added: "mot Temp"
- board text added: "motor TEMP"
- board text removed: "- U +"
- board text removed: "- V +"
- board text removed: "- W +"
- board text removed: "-3V3 -GND -5V -GND -24V -24V -GND -T_V -T_U -WL -VL -UL -UH -VH -WH"
- board text removed: "24V prefuse"
- board text removed: "3V3"
- board text removed: "3V3- GND- 5V- GND- 24V- 24V- GND- FLTN- GDY- GATE_EN- Vsense_W- Vsense_V- Vsense_U- Vsense_DC- T_W-"
- board text removed: "BOOT0"
- board text removed: "CAN1"
- board text removed: "CAN1_STB"
- board text removed: "CAN2"
- board text removed: "CAN2_STB"
- board text removed: "COS"
- board text removed: "COS+"
- board text removed: "COS-"
- board text removed: "DC GND - + +5V"
- board text removed: "DEBUG"
- board text removed: "EP6 INV_MainBoard_STM32 V1.0 24/11/16 Jack Kuo"
- board text removed: "FLTN"
- board text removed: "FX26-30P-1SV"
- board text removed: "GATE_EN"
- board text removed: "GATE_ENC"
- board text removed: "GND"
- board text removed: "GND COS- COS+ COS- SIN- SIN+ +5V T_mot GND"
- board text removed: "GND H L 5V"
- board text removed: "H L"
- board text removed: "I_DC"
- board text removed: "I_U"
- board text removed: "I_V"
- board text removed: "I_W"
- board text removed: "Isense 4-20mA"
- board text removed: "Isense ISB-100-A-802"
- board text removed: "PA0"
- board text removed: "PA1"
- board text removed: "PA2"
- board text removed: "PB10"
- board text removed: "PB15"
- board text removed: "PC0"
- board text removed: "PC15"
- board text removed: "PC6"
- board text removed: "PC7"
- board text removed: "RDY"
- board text removed: "SCL"
- board text removed: "SDA"
- board text removed: "SIN"
- board text removed: "SIN+"
- board text removed: "SIN-"
- board text removed: "T_U"
- board text removed: "T_V"
- board text removed: "T_W"
- board text removed: "T_mot"
- board text removed: "U GND - + +5V"
- board text removed: "UH VH WH"
- board text removed: "UL VL WL"
- board text removed: "V GND - + +5V"
- board text removed: "V_DC"
- board text removed: "V_U"
- board text removed: "V_V"
- board text removed: "V_W"
- board text removed: "W GND - + +5V"
- board text removed: "W V U"
- board text removed: "encoder & T_Mot"

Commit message: update INV_MainBoard_STM32 to V2.1
update for JLCPCB, include change in 1.65 Vref and some name change for easier JLCPCBA BOM selection
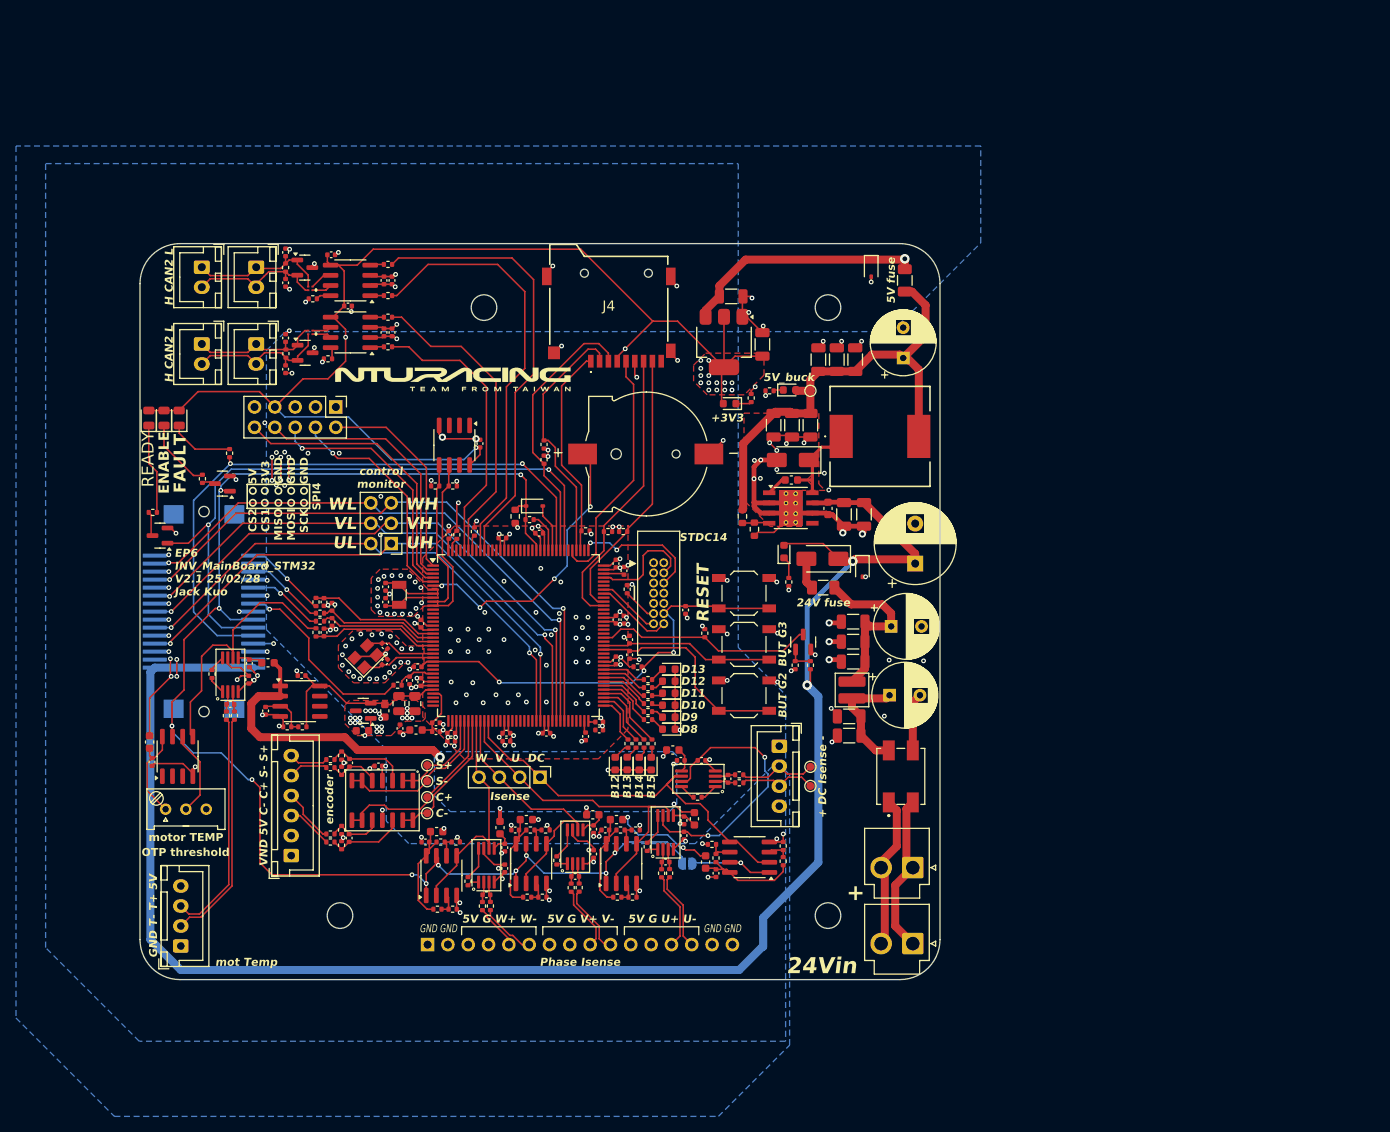
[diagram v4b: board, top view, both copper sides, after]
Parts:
- removed FB4: GZ1608D601TF, Capacitor_SMD:C_0603_1608Metric
- JP1: moved to B.Cu
- R15, R16, R70, R71: value 20R -> 22R
- U10, U11, U12, U13, U15: value LM2903 -> LM393
- U18: value OPA340NA -> NE5532; footprint Package_TO_SOT_SMD:SOT-23-5 -> Package_SO:SOIC-8_3.9x4.9mm_P1.27mm
- U23: value REF3133AQDBZRQ1 -> REF3133AIDBZR
- U5: value CAT24C256 -> CAT24C512
- moved C103 62.3 mm to (128.7, 111.0), turned to 180 degrees
- moved C104 61.3 mm to (124.2, 115.4), turned to -90 degrees
- moved U18 59.5 mm to (128.5, 114.2), turned to 0 degrees
- moved R25 58.2 mm to (128.8, 117.4)
- moved R26 57.1 mm to (126.9, 117.4), turned to 180 degrees
- moved R81 12.1 mm to (147.6, 87.3), turned to 180 degrees
- moved R82 9.65 mm to (145.4, 87.3), turned to 0 degrees
- moved FB6 7.14 mm to (175.1, 120.3), turned to 180 degrees
- moved C35 5.76 mm to (151.0, 82.0)
- moved U5 5.76 mm to (147.8, 82.2)
- moved FB11 5.32 mm to (109.7, 119.3), turned to -90 degrees
- moved C46 5.19 mm to (180.5, 135.7)
- moved R29 5.19 mm to (188.9, 134.2)
- moved R30 5.19 mm to (188.9, 132.3)
- moved R54 5.19 mm to (180.5, 133.8)
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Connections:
- C103 pad 1: Net-(U18-V+) -> /MCU/VDDA_REF
- FB11 pad 1: +3V3 -> +5V
- R25 pad 1: Net-(U18-V+) -> /MCU/VDDA_REF
- U18 pad 2: GND -> /Isense&motT_OCP&OTP/Vref_1.65V
- U18 pad 4: /Isense&motT_OCP&OTP/Vref_1.65V -> GND
- U18 pad 5: Net-(U18-V+) -> unconnected-(U18B-+-Pad5)
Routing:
- net /Isense&motT_OCP&OTP/Vref_1.65V: track 94.3 -> 43.2 mm, vias 7 -> 5
- net /MCU/VDDA_REF: track 9.47 -> 24.6 mm
- net +5V: track 90.3 -> 105.2 mm, vias 16 -> 14
- net +3V3: track 215.9 -> 227.2 mm, vias 45 -> 73
- net /MCU/I2C2_SCL: track 30.7 -> 20.7 mm
- net GND: track 264.4 -> 256.8 mm, vias 196 -> 228
- net /MCU/I2C2_SDA: track 26.9 -> 19.4 mm
- net Net-(U18-V+): track 5.20 -> 0.00 mm
- net Net-(U7-REF): track 7.12 -> 3.08 mm
- net /Isense&motT_OCP&OTP/Isense_DC: track 53.6 -> 50.0 mm
- net Net-(U15B--): track 7.30 -> 10.7 mm
- net /Isense&motT_OCP&OTP/filt3V3: track 15.2 -> 12.4 mm
- net /GATE_EN: track 182.8 -> 185.5 mm, vias 13 -> 12
- net /Isense&motT_OCP&OTP/MotTempNode/IN-: track 31.9 -> 29.4 mm
- net /Isense&motT_OCP&OTP/MotTempNode/IN+: track 31.0 -> 28.7 mm
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- added copper zone on B.Cu, net /Isense&motT_OCP&OTP/Vref_1.65V
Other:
- board text added: "EP6 INV_MainBoard_STM32 V2.1 25/02/28 Jack Kuo"
- board text removed: "EP6 INV_MainBoard_STM32 V2.0 25/02/28 Jack Kuo"
